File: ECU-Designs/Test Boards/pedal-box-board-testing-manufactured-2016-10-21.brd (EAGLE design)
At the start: 72.4 x 67 mm, 29 parts, among them X1 MINIFIT_5566-4, X2 MINIFIT_5566-4

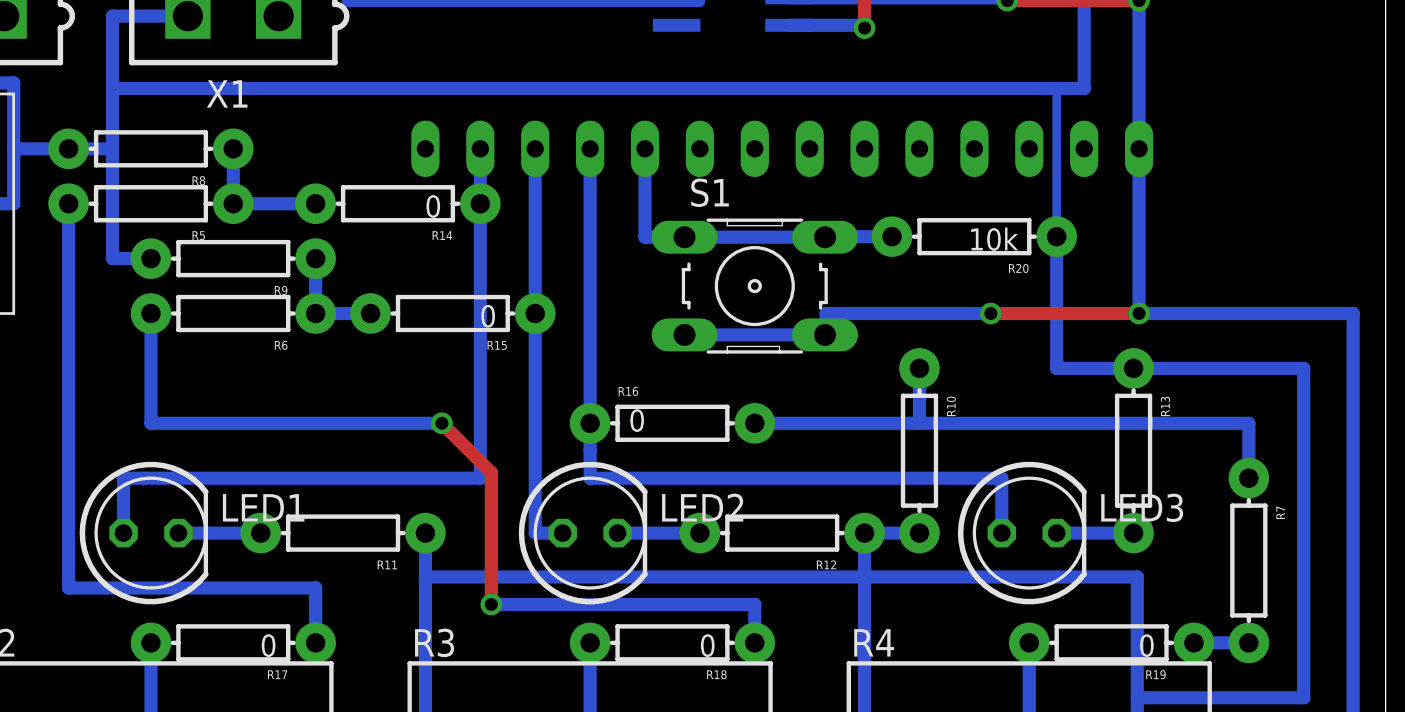
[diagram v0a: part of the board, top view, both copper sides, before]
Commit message: Add buzzer, CD chips, mosfet to HyTechDevices library, changes to pedal testing board
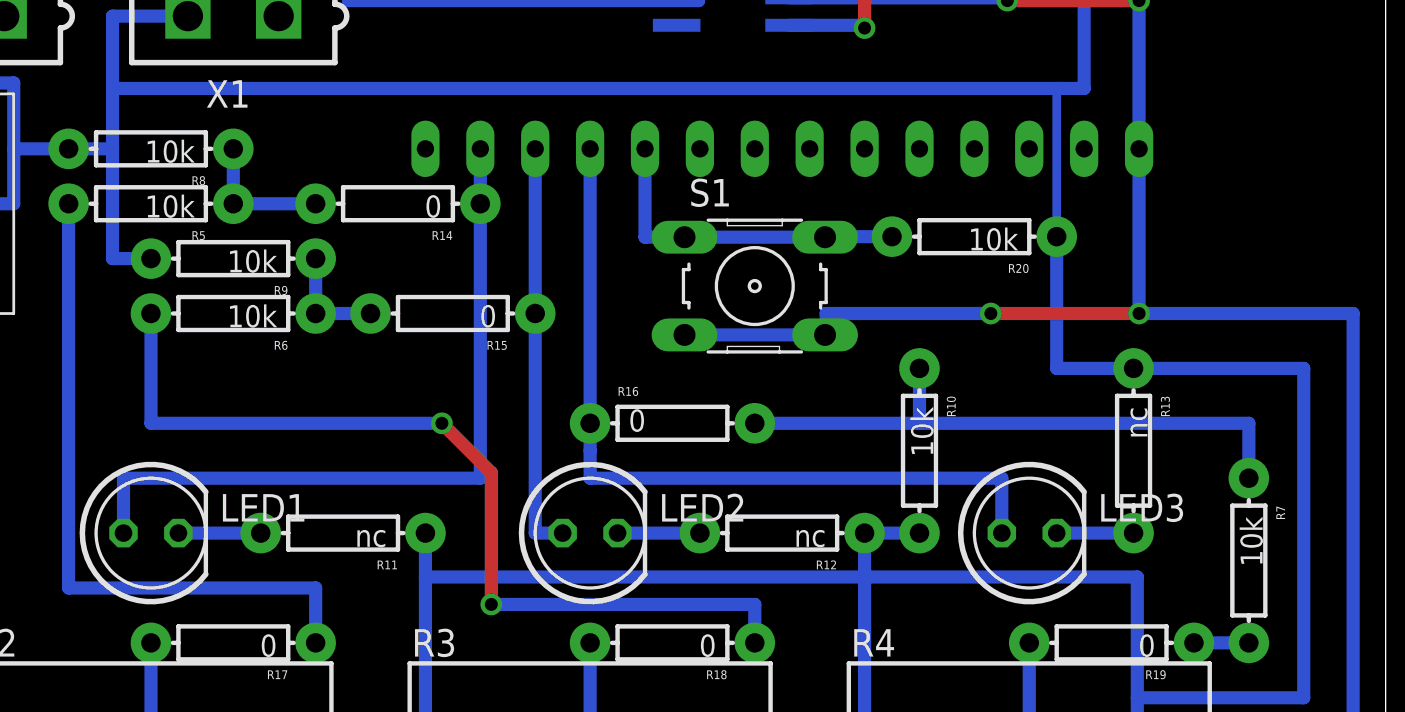
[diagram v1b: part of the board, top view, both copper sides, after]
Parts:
- R10, R5, R6, R7, R8, R9: value (none) -> 10k
- R11, R12, R13: value (none) -> nc
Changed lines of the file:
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@@
 <element name="R3" library="HyTechDevices" package="3RP/1610N" value="" x="35.56" y="15.24"/>
 <element name="R4" library="HyTechDevices" package="3RP/1610N" value="" x="55.88" y="15.24"/>
-<element name="R5" library="HyTechDevices" package="AXIAL-0.3EZ" value="" x="15.24" y="41.91" rot="R180"/>
-<element name="R6" library="HyTechDevices" package="AXIAL-0.3EZ" value="" x="19.05" y="36.83" rot="R180"/>
-<element name="R7" library="HyTechDevices" package="AXIAL-0.3EZ" value="" x="66.04" y="25.4" rot="R270"/>
-<element name="R8" library="HyTechDevices" package="AXIAL-0.3EZ" value="" x="15.24" y="44.45" rot="R180"/>
-<element name="R9" library="HyTechDevices" package="AXIAL-0.3EZ" value="" x="19.05" y="39.37" rot="R180"/>
-<element name="R10" library="HyTechDevices" package="AXIAL-0.3EZ" value="" x="50.8" y="30.48" rot="R270"/>
+<element name="R5" library="HyTechDevices" package="AXIAL-0.3EZ" value="10k" x="15.24" y="41.91" rot="R180"/>
+<element name="R6" library="HyTechDevices" package="AXIAL-0.3EZ" value="10k" x="19.05" y="36.83" rot="R180"/>
+<element name="R7" library="HyTechDevices" package="AXIAL-0.3EZ" value="10k" x="66.04" y="25.4" rot="R270"/>
+<element name="R8" library="HyTechDevices" package="AXIAL-0.3EZ" value="10k" x="15.24" y="44.45" rot="R180"/>
+<element name="R9" library="HyTechDevices" package="AXIAL-0.3EZ" value="10k" x="19.05" y="39.37" rot="R180"/>
+<element name="R10" library="HyTechDevices" package="AXIAL-0.3EZ" value="10k" x="50.8" y="30.48" rot="R270"/>
 <element name="LED1" library="HyTechDevices" package="LED-5MM" value="" x="15.24" y="26.67"/>
 <element name="LED2" library="HyTechDevices" package="LED-5MM" value="" x="35.56" y="26.67"/>
 <element name="LED3" library="HyTechDevices" package="LED-5MM" value="" x="55.88" y="26.67"/>
-<element name="R11" library="HyTechDevices" package="AXIAL-0.3EZ" value="" x="24.13" y="26.67" rot="R180"/>
-<element name="R12" library="HyTechDevices" package="AXIAL-0.3EZ" value="" x="44.45" y="26.67" rot="R180"/>
-<element name="R13" library="HyTechDevices" package="AXIAL-0.3EZ" value="" x="60.706" y="30.48" rot="R270"/>
+<element name="R11" library="HyTechDevices" package="AXIAL-0.3EZ" value="nc" x="24.13" y="26.67" rot="R180"/>
+<element name="R12" library="HyTechDevices" package="AXIAL-0.3EZ" value="nc" x="44.45" y="26.67" rot="R180"/>
+<element name="R13" library="HyTechDevices" package="AXIAL-0.3EZ" value="nc" x="60.706" y="30.48" rot="R270"/>
 <element name="R14" library="HyTechDevices" package="AXIAL-0.3EZ" value="0" x="26.67" y="41.91" rot="R180"/>
 <element name="R15" library="HyTechDevices" package="AXIAL-0.3EZ" value="0" x="29.21" y="36.83" rot="R180"/>
